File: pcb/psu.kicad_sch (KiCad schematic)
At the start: 20 parts, among them J1 PZ254V-11-02P, U4 DC-005H-D020, U5 LMR16010

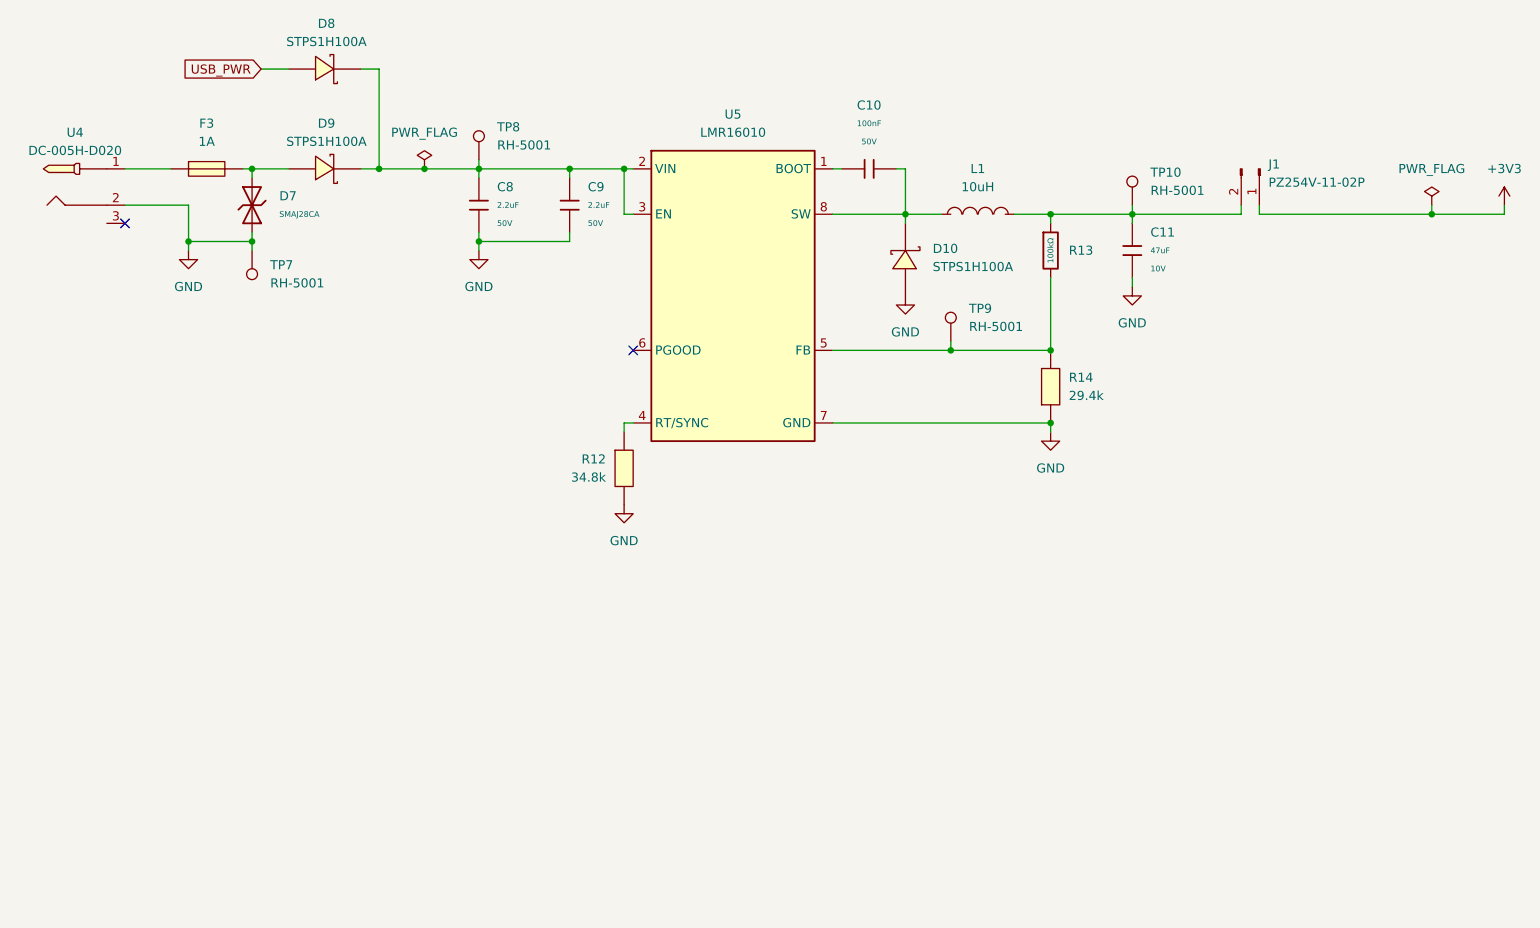
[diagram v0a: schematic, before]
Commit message: feat: replace many parts for basic parts
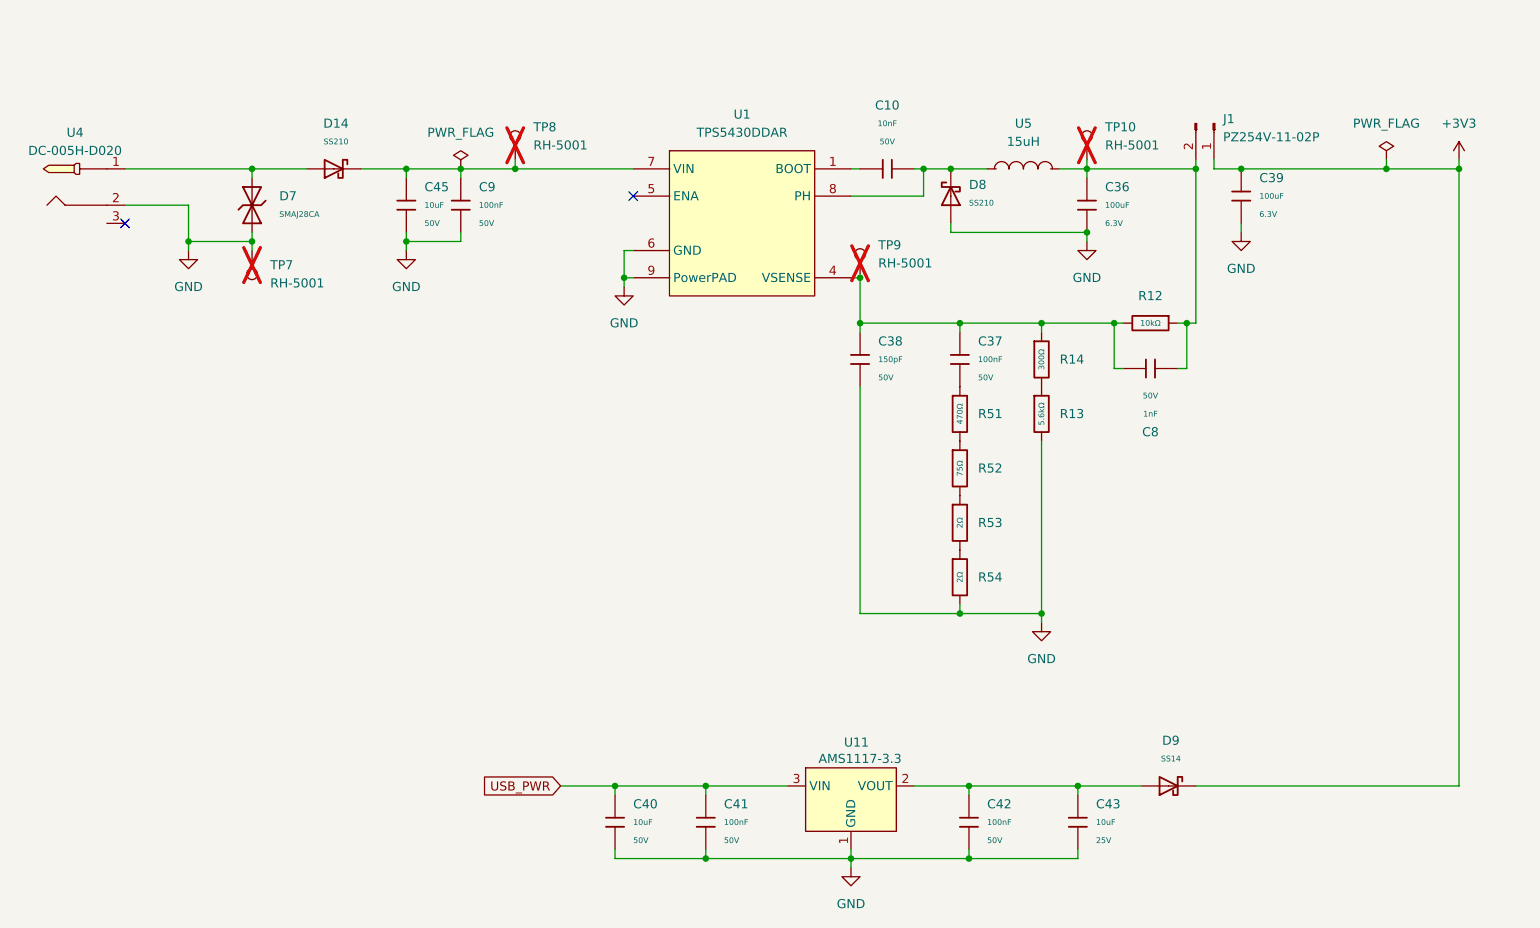
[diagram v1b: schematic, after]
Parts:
- removed C10: 100nF, PCM_JLCPCB:C_0603, symbol PCM_JLCPCB-Capacitors:0603,100nF
- removed C11: 47uF, PCM_JLCPCB:C_1206, symbol PCM_JLCPCB-Capacitors:1206,47uF
- removed C8, C9: 2.2uF, PCM_JLCPCB:C_1206, symbol PCM_JLCPCB-Capacitors:1206,2.2uF
- removed D10, D8, D9: STPS1H100A, EasyEDA:SMA_L4.3-W2.6-LS5.2-RD, symbol EasyEDA:STPS1H100A
- removed F3: 1A, EasyEDA:F1206, symbol EasyEDA:BSMD1206C-1100T
- removed L1: 10uH, EasyEDA:IND-SMD_L4.0-W4.0_FNR40XXS, symbol EasyEDA:FNR4030S100MT
- removed R12: 34.8k, EasyEDA:R0603, symbol EasyEDA:FRC0603F3482TS
- removed R13: 100kΩ, PCM_JLCPCB:R_0603, symbol PCM_JLCPCB-Resistors:0603,100kΩ
- removed R14: 29.4k, EasyEDA:R0603, symbol EasyEDA:FRC0603F2942TS
- removed U5: LMR16010, EasyEDA:SOPOWERPAD-8_L4.9-W3.9-P1.27-LS6.0-BL-EP, symbol custom_symbols:LMR16010
- added C10: 10nF, PCM_JLCPCB:C_0603, symbol PCM_JLCPCB-Capacitors:0603,10nF
- added C36, C39: 100uF, PCM_JLCPCB:C_1206, symbol PCM_JLCPCB-Capacitors:1206,100uF
- added C37, C41, C42, C9: 100nF, PCM_JLCPCB:C_0603, symbol PCM_JLCPCB-Capacitors:0603,100nF
- added C38: 150pF, PCM_JLCPCB:C_0603, symbol PCM_JLCPCB-Capacitors:0603,150pF
- added C40: 10uF, PCM_JLCPCB:C_1206, symbol PCM_JLCPCB-Capacitors:1206,10uF
- added C43: 10uF, PCM_JLCPCB:C_0603, symbol PCM_JLCPCB-Capacitors:0603,10uF,(2)
- added C45: 10uF, PCM_JLCPCB:C_0805, symbol PCM_JLCPCB-Capacitors:0805,10uF,(2)
- added C8: 1nF, PCM_JLCPCB:C_0603, symbol PCM_JLCPCB-Capacitors:0603,1nF
- added D14, D8: SS210, PCM_JLCPCB:D_SMA, symbol PCM_JLCPCB-Diodes:Schottky,SS210
- added D9: SS14, PCM_JLCPCB:D_SMA, symbol PCM_JLCPCB-Diodes:Schottky,SS14
- added R12: 10kΩ, PCM_JLCPCB:R_0603, symbol PCM_JLCPCB-Resistors:0603,10kΩ
- added R13: 5.6kΩ, PCM_JLCPCB:R_0603, symbol PCM_JLCPCB-Resistors:0603,5.6kΩ
- added R14: 300Ω, PCM_JLCPCB:R_0603, symbol PCM_JLCPCB-Resistors:0603,300Ω
- added R51: 470Ω, PCM_JLCPCB:R_0603, symbol PCM_JLCPCB-Resistors:0603,470Ω
- added R52: 75Ω, PCM_JLCPCB:R_0603, symbol PCM_JLCPCB-Resistors:0603,75Ω
- added R53, R54: 2Ω, PCM_JLCPCB:R_0603, symbol PCM_JLCPCB-Resistors:0603,2Ω
- added U1: TPS5430DDAR, EasyEDA:ESOP-8_L4.9-W3.9-P1.27-LS6.0-TL-EP, symbol EasyEDA:TPS5430DDAR
- added U11: AMS1117-3.3, EasyEDA:SOT-223_L6.5-W3.5-P2.30-LS7.0-BR, symbol EasyEDA:AMS1117-5.0
- added U5: 15uH, EasyEDA:IND-SMD_L7.1-W6.6, symbol EasyEDA:APH0630T150M
- TP10, TP7, TP8, TP9: now not fitted; now left out of the parts list
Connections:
- net +3V3: now also C39.1, D9.1
- net GND: now also C36.2, C38.2, C39.2, C40.2, C41.2, C42.2, C43.2, C45.2, C9.2, D8.2, R13.2, R54.2, U1.6 (GND), U1.9 (PowerPAD), U11.1 (GND)
- net USB_PWR: now also C40.1, C41.1, U11.3 (VIN)
- net at TP8.1: now also C45.1, C9.1, D14.1, U1.7 (VIN)
- net at D7.2: now also U4.1, D14.2
- net at TP9.1: now also C37.1, C38.1, C8.2, R12.2, R14.1, U1.4 (VSENSE)
- net at J1.2 (Pin_2), TP10.1: now also C36.1, C8.1, R12.1, U5.2
- new net: C10.1, U1.1 (BOOT)
- new net: C10.2, D8.1, U1.8 (PH), U5.1
- new net: R13.1, R14.2
- new net: C37.2, R51.1
- new net: C42.1, C43.1, D9.2, U11.2 (VOUT)
- new net: R51.2, R52.1
- new net: R52.2, R53.1
- new net: R53.2, R54.1
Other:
- moved on the sheet: J1

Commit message: pcb: update symbols and footprints to fix drc
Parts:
- C10: Price 0.005USD -> 0.006USD; Stock 5921160 -> 2223405
- C36, C39: Price 0.066USD -> 0.060USD; Stock 1472723 -> 1652143
- C37, C41, C42, C9: Stock 70324515 -> 37493696
- C38: Stock 179177 -> 457309
- C40: Price 0.035USD -> 0.061USD; Stock 3698334 -> 1900877
- C43: Price 0.021USD -> 0.020USD; Stock 3388297 -> 3475471
- C45: Price 0.066USD -> 0.070USD; Stock 1422246 -> 1940473
- C8: Stock 6068974 -> 15568229
- D14, D8: Price 0.029USD -> 0.030USD; Stock 272493 -> 1058068
- D7: footprint PCM_JLCPCB:D_SMA -> PCM_JLCPCB:D_DO-214AC(SMA); Price 0.038USD -> 0.039USD; Stock 103246 -> 77690
- D9: Price 0.018USD -> 0.019USD; Stock 1115112 -> 1664025
- R12: Price 0.004USD -> 0.005USD; Stock 51181774 -> 22319909
- R13: Stock 401557 -> 785954
- R14: Price 0.004USD -> 0.005USD; Stock 372967 -> 1130466
- R51: Price 0.004USD -> 0.005USD; Stock 3910258 -> 2978459
- R52: Price 0.004USD -> 0.005USD; Stock 985553 -> 2923669
- R53, R54: Stock 880724 -> 235771
- U11: LCSC Part C6186 -> C6187; MPN AMS1117-3.3 -> AMS1117-5.0
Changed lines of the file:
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@@
 			)
 		)
-		(property "Stock" "5921160"
+		(property "Stock" "2223405"
 			(at 165.1 52.07 0)
 			(hide yes)
@@
 			)
 		)
-		(property "Price" "0.005USD"
+		(property "Price" "0.006USD"
 			(at 165.1 52.07 0)
 			(hide yes)
@@
 			)
 		)
-		(property "Description" "100V 850mV@2A 2A SMA(DO-214AC) Schottky Diodes ROHS"
+		(property "Description" "-55°C~+150°C 1 Independent 100V 2A 500uA@100V 850mV@2A SMA(DO-214AC) Schottky Diodes ROHS"
 			(at 87.63 52.07 0)
 			(hide yes)
@@
 			)
 		)
-		(property "Stock" "272493"
+		(property "Stock" "1058068"
 			(at 87.63 52.07 0)
 			(hide yes)
@@
 			)
 		)
-		(property "Price" "0.029USD"
+		(property "Price" "0.030USD"
 			(at 87.63 52.07 0)
 			(hide yes)
@@
 			)
 		)
-		(property "Stock" "401557"
+		(property "Stock" "785954"
 			(at 186.69 86.36 0)
 			(hide yes)
@@
 			)
 		)
-		(property "Stock" "372967"
+		(property "Stock" "1130466"
 			(at 186.69 78.74 0)
 			(hide yes)
@@
 			)
 		)
-		(property "Price" "0.004USD"
+		(property "Price" "0.005USD"
 			(at 186.69 78.74 0)
 			(hide yes)
@@
 			)
 		)
-		(property "Stock" "51181774"
+		(property "Stock" "22319909"
 			(at 201.93 73.66 0)
 			(hide yes)
@@
 			)
 		)
-		(property "Price" "0.004USD"
+		(property "Price" "0.005USD"
 			(at 201.93 73.66 0)
 			(hide yes)
@@
 			)
 		)
-		(property "Stock" "70324515"
+		(property "Stock" "37493696"
 			(at 175.26 78.74 0)
 			(hide yes)
@@
 			)
 		)
-		(property "Stock" "1115112"
+		(property "Stock" "1664025"
 			(at 204.47 138.43 0)
 			(hide yes)
@@
 			)
 		)
-		(property "Price" "0.018USD"
+		(property "Price" "0.019USD"
 			(at 204.47 138.43 0)
 			(hide yes)
@@
 			)
 		)
-		(property "Stock" "985553"
+		(property "Stock" "2923669"
 			(at 175.26 93.98 0)
 			(hide yes)
@@
 			)
 		)
-		(property "Price" "0.004USD"
+		(property "Price" "0.005USD"
 			(at 175.26 93.98 0)
 			(hide yes)
@@
 			)
 		)
-		(property "Stock" "272493"
+		(property "Stock" "1058068"
 			(at 173.99 55.88 0)
 			(hide yes)
@@
 			)
 		)
-		(property "Price" "0.029USD"
+		(property "Price" "0.030USD"
 			(at 173.99 55.88 0)
 			(hide yes)
@@
 			)
 		)
-		(property "MPN" "AMS1117-3.3"
+		(property "MPN" "AMS1117-5.0"
 			(at 162.56 157.48 0)
 			(hide yes)
@@
 			)
 		)
-		(property "LCSC Part" "C6186"
+		(property "LCSC Part" "C6187"
 			(at 162.56 160.02 0)
 			(hide yes)
@@
 			)
 		)
-		(property "Stock" "70324515"
+		(property "Stock" "37493696"
 			(at 105.41 57.15 0)
 			(hide yes)
@@
 			)
 		)
-		(property "Stock" "1472723"
+		(property "Stock" "1652143"
 			(at 214.63 55.88 0)
 			(hide yes)
@@
 			)
 		)
-		(property "Price" "0.066USD"
+		(property "Price" "0.060USD"
 			(at 214.63 55.88 0)
 			(hide yes)
@@
 			)
 		)
-		(property "Footprint" "PCM_JLCPCB:D_SMA"
+		(property "Footprint" "PCM_JLCPCB:D_DO-214AC(SMA)"
 			(at 74.422 57.15 90)
 			(hide yes)
@@
 			)
 		)
-		(property "Description" "8.8A 45.4V 400W 34.4V Bidirectional 28V SMA ESD and Surge Protection (TVS/ESD) ROHS"
+		(property "Description" "-55°C~+150°C 1uA 28V 34.4V 400W@10/1000us 45.4V 8.8A Bidirectional IEC 61000-4-2 TVS DO-214AC(SMA) ESD and Surge Protection (TVS/ESD) ROHS"
 			(at 76.2 57.15 0)
 			(hide yes)
@@
 			)
 		)
-		(property "Stock" "103246"
+		(property "Stock" "77690"
 			(at 76.2 57.15 0)
 			(hide yes)
@@
 			)
 		)
-		(property "Price" "0.038USD"
+		(property "Price" "0.039USD"
 			(at 76.2 57.15 0)
 			(hide yes)
@@
 			)
 		)
-		(property "Stock" "880724"
+		(property "Stock" "235771"
 			(at 175.26 109.22 0)
 			(hide yes)
@@
 			)
 		)
-		(property "Stock" "6068974"
+		(property "Stock" "15568229"
 			(at 201.93 80.01 0)
 			(hide yes)
@@
 			)
 		)
-		(property "Stock" "179177"
+		(property "Stock" "457309"
 			(at 161.29 78.74 0)
 			(hide yes)
@@
 			)
 		)
-		(property "Stock" "1472723"
+		(property "Stock" "1652143"
 			(at 193.04 57.15 0)
 			(hide yes)
@@
 			)
 		)
-		(property "Price" "0.066USD"
+		(property "Price" "0.060USD"
 			(at 193.04 57.15 0)
 			(hide yes)
@@
 			)
 		)
-		(property "Stock" "3698334"
+		(property "Stock" "1900877"
 			(at 127 143.51 0)
 			(hide yes)
@@
 			)
 		)
-		(property "Price" "0.035USD"
+		(property "Price" "0.061USD"
 			(at 127 143.51 0)
 			(hide yes)
@@
 			)
 		)
-		(property "Description" "50V 10uF X5R ±10% 0805 Multilayer Ceramic Capacitors MLCC - SMD/SMT ROHS"
+		(property "Description" "10uF 50V X5R ±10% 0805 Multilayer Ceramic Capacitors MLCC - SMD/SMT ROHS"
 			(at 97.79 57.15 0)
 			(hide yes)
@@
 			)
 		)
-		(property "Stock" "1422246"
+		(property "Stock" "1940473"
 			(at 97.79 57.15 0)
 			(hide yes)
@@
 			)
 		)
-		(property "Price" "0.066USD"
+		(property "Price" "0.070USD"
 			(at 97.79 57.15 0)
 			(hide yes)
@@
 			)
 		)
-		(property "Stock" "70324515"
+		(property "Stock" "37493696"
 			(at 139.7 143.51 0)
 			(hide yes)
@@
 			)
 		)
-		(property "Stock" "3910258"
+		(property "Stock" "2978459"
 			(at 175.26 86.36 0)
 			(hide yes)
@@
 			)
 		)
-		(property "Price" "0.004USD"
+		(property "Price" "0.005USD"
 			(at 175.26 86.36 0)
 			(hide yes)
@@
 			)
 		)
-		(property "Stock" "3388297"
+		(property "Stock" "3475471"
 			(at 191.77 143.51 0)
 			(hide yes)
@@
 			)
 		)
-		(property "Price" "0.021USD"
+		(property "Price" "0.020USD"
 			(at 191.77 143.51 0)
 			(hide yes)
@@
 			)
 		)
-		(property "Stock" "880724"
+		(property "Stock" "235771"
 			(at 175.26 101.6 0)
 			(hide yes)
@@
 			)
 		)
-		(property "Stock" "70324515"
+		(property "Stock" "37493696"
 			(at 176.53 143.51 0)
 			(hide yes)
